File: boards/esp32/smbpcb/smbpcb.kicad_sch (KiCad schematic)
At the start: 69 parts, among them IC1 MiCS-6814, J1 USB_B_Micro, J2 PMS7003, Q1 SUD08P06-155L, Q2 SS8050_NPN, Q3 SS8050_NPN, SW1 RESET, SW2 RESET, U1 MCP73831-2-OT, U2 TPS61200DRC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

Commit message: assembly QOL improvements
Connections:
- net +5V: now also R25.1; no longer R25.2
- net GND: now also D3.1 (K)
- net at D3.2 (A): now also R25.2; no longer R25.1
- net at C5.1, D1.1 (K): no longer D3.1 (K)
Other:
- moved on the sheet: D3, R25
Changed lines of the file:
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@@
   (junction (at 180.34 58.42) (diameter 0.9144) (color 0 0 0 0))
   (junction (at 185.42 80.01) (diameter 0.9144) (color 0 0 0 0))
-  (junction (at 189.23 21.59) (diameter 0.9144) (color 0 0 0 0))
-  (junction (at 189.23 58.42) (diameter 0.9144) (color 0 0 0 0))
   (junction (at 192.405 168.91) (diameter 0.9144) (color 0 0 0 0))
+  (junction (at 198.12 80.01) (diameter 0.9144) (color 0 0 0 0))
   (junction (at 201.93 138.43) (diameter 0.9144) (color 0 0 0 0))
+  (junction (at 212.09 58.42) (diameter 0.9144) (color 0 0 0 0))
   (junction (at 215.265 120.65) (diameter 0.9144) (color 0 0 0 0))
   (junction (at 222.885 120.65) (diameter 0.9144) (color 0 0 0 0))
@@
     (stroke (width 0) (type solid) (color 0 0 0 0))
   )
-  (wire (pts (xy 165.1 21.59) (xy 189.23 21.59))
+  (wire (pts (xy 165.1 21.59) (xy 198.12 21.59))
     (stroke (width 0) (type solid) (color 0 0 0 0))
   )
@@
     (stroke (width 0) (type solid) (color 0 0 0 0))
   )
-  (wire (pts (xy 180.34 58.42) (xy 189.23 58.42))
+  (wire (pts (xy 180.34 58.42) (xy 212.09 58.42))
     (stroke (width 0) (type solid) (color 0 0 0 0))
   )
@@
     (stroke (width 0) (type solid) (color 0 0 0 0))
   )
-  (wire (pts (xy 189.23 21.59) (xy 189.23 33.02))
-    (stroke (width 0) (type solid) (color 0 0 0 0))
-  )
-  (wire (pts (xy 189.23 21.59) (xy 198.12 21.59))
-    (stroke (width 0) (type solid) (color 0 0 0 0))
-  )
-  (wire (pts (xy 189.23 40.64) (xy 189.23 44.45))
-    (stroke (width 0) (type solid) (color 0 0 0 0))
-  )
-  (wire (pts (xy 189.23 52.07) (xy 189.23 58.42))
-    (stroke (width 0) (type solid) (color 0 0 0 0))
-  )
-  (wire (pts (xy 189.23 58.42) (xy 215.9 58.42))
-    (stroke (width 0) (type solid) (color 0 0 0 0))
-  )
   (wire (pts (xy 189.23 135.89) (xy 189.23 139.7))
     (stroke (width 0) (type solid) (color 0 0 0 0))
@@
     (stroke (width 0) (type solid) (color 0 0 0 0))
   )
+  (wire (pts (xy 198.12 82.55) (xy 198.12 80.01))
+    (stroke (width 0) (type solid) (color 0 0 0 0))
+  )
   (wire (pts (xy 199.39 135.89) (xy 199.39 139.7))
     (stroke (width 0) (type solid) (color 0 0 0 0))
@@
   )
   (wire (pts (xy 201.93 168.91) (xy 205.74 168.91))
+    (stroke (width 0) (type solid) (color 0 0 0 0))
+  )
+  (wire (pts (xy 212.09 58.42) (xy 212.09 64.77))
+    (stroke (width 0) (type solid) (color 0 0 0 0))
+  )
+  (wire (pts (xy 212.09 58.42) (xy 215.9 58.42))
+    (stroke (width 0) (type solid) (color 0 0 0 0))
+  )
+  (wire (pts (xy 212.09 72.39) (xy 212.09 74.93))
+    (stroke (width 0) (type solid) (color 0 0 0 0))
+  )
+  (wire (pts (xy 212.09 82.55) (xy 198.12 82.55))
     (stroke (width 0) (type solid) (color 0 0 0 0))
   )
@@
     (pin "2")
   )
-  (symbol (lib_id "Device:R") (at 189.23 48.26 0) (unit 1)
-    (in_bom yes) (on_board yes)
-    (property "Reference" "R25" (id 0) (at 189.865 44.45 0)
-      (effects (font (size 1.27 1.27)) (justify left))
-    )
-    (property "Value" "2k" (id 1) (at 189.865 52.07 0)
-      (effects (font (size 1.27 1.27)) (justify left))
-    )
-    (property "Footprint" "Capacitor_SMD:C_0805_2012Metric" (id 2) (at 187.452 48.26 90)
-      (effects (font (size 1.27 1.27)) hide)
-    )
-    (property "Datasheet" "~" (id 3) (at 189.23 48.26 0)
-      (effects (font (size 1.27 1.27)) hide)
-    )
-    (property "LCSC" "C328391" (id 4) (at 189.23 48.26 0)
-      (effects (font (size 1.27 1.27)) hide)
-    )
-    (property "Mouser" "AECR0805F2K00K9" (id 5) (at 189.23 48.26 0)
-      (effects (font (size 1.27 1.27)) hide)
-    )
-    (pin "1")
-    (pin "2")
-  )
   (symbol (lib_id "Device:R") (at 198.12 168.91 90) (unit 1)
     (in_bom yes) (on_board yes)
@@
     (pin "2")
   )
+  (symbol (lib_id "Device:R") (at 212.09 68.58 0) (unit 1)
+    (in_bom yes) (on_board yes)
+    (property "Reference" "R25" (id 0) (at 212.725 64.77 0)
+      (effects (font (size 1.27 1.27)) (justify left))
+    )
+    (property "Value" "2k" (id 1) (at 212.725 72.39 0)
+      (effects (font (size 1.27 1.27)) (justify left))
+    )
+    (property "Footprint" "Capacitor_SMD:C_0805_2012Metric" (id 2) (at 210.312 68.58 90)
+      (effects (font (size 1.27 1.27)) hide)
+    )
+    (property "Datasheet" "~" (id 3) (at 212.09 68.58 0)
+      (effects (font (size 1.27 1.27)) hide)
+    )
+    (property "LCSC" "C328391" (id 4) (at 212.09 68.58 0)
+      (effects (font (size 1.27 1.27)) hide)
+    )
+    (property "Mouser" "AECR0805F2K00K9" (id 5) (at 212.09 68.58 0)
+      (effects (font (size 1.27 1.27)) hide)
+    )
+    (pin "1")
+    (pin "2")
+  )
   (symbol (lib_id "Device:R") (at 215.265 128.905 0) (unit 1)
     (in_bom yes) (on_board yes)
@@
     (pin "2")
   )
-  (symbol (lib_id "Device:LED") (at 189.23 36.83 270) (unit 1)
-    (in_bom yes) (on_board yes)
-    (property "Reference" "D3" (id 0) (at 191.77 36.195 90)
-      (effects (font (size 1.27 1.27)) (justify left))
-    )
-    (property "Value" "PWR_LED" (id 1) (at 191.77 38.735 90)
-      (effects (font (size 1.27 1.27)) (justify left))
-    )
-    (property "Footprint" "LED_SMD:LED_0805_2012Metric" (id 2) (at 189.23 36.83 0)
-      (effects (font (size 1.27 1.27)) hide)
-    )
-    (property "Datasheet" "~" (id 3) (at 189.23 36.83 0)
-      (effects (font (size 1.27 1.27)) hide)
-    )
-    (property "LCSC" "C72037" (id 4) (at 189.23 36.83 0)
-      (effects (font (size 1.27 1.27)) hide)
-    )
-    (property "Mouser" " 755-SML-H12U8TT86C " (id 5) (at 189.23 36.83 0)
-      (effects (font (size 1.27 1.27)) hide)
-    )
+  (symbol (lib_id "Device:LED") (at 212.09 78.74 90) (unit 1)
+    (in_bom yes) (on_board yes)
+    (property "Reference" "D3" (id 0) (at 209.55 79.375 90)
+      (effects (font (size 1.27 1.27)) (justify left))
+    )
+    (property "Value" "PWR_LED" (id 1) (at 209.55 76.835 90)
+      (effects (font (size 1.27 1.27)) (justify left))
+    )
+    (property "Footprint" "LED_SMD:LED_0805_2012Metric" (id 2) (at 212.09 78.74 0)
+      (effects (font (size 1.27 1.27)) hide)
+    )
+    (property "Datasheet" "~" (id 3) (at 212.09 78.74 0)
+      (effects (font (size 1.27 1.27)) hide)
+    )
+    (property "LCSC" "C72037" (id 4) (at 212.09 78.74 0)
+      (effects (font (size 1.27 1.27)) hide)
+    )
+    (property "Mouser" " 755-SML-H12U8TT86C " (id 5) (at 212.09 78.74 0)
+      (effects (font (size 1.27 1.27)) hide)
+    )

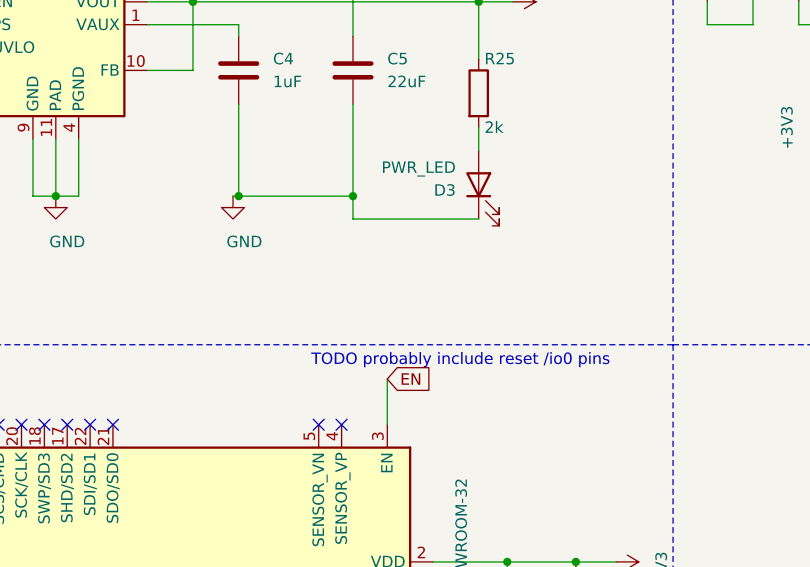
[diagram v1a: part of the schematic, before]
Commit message: wrong micro usb footprint
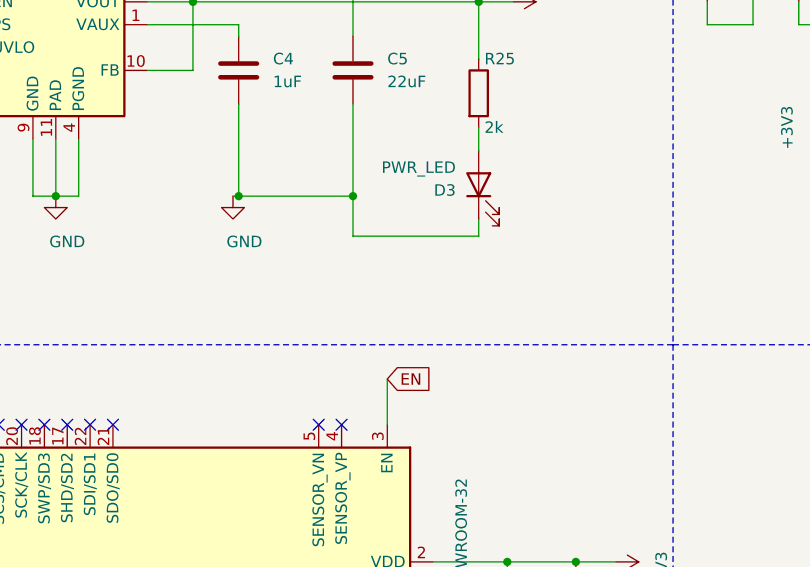
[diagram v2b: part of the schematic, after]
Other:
- note removed: "TODO probably include reset /io0 pins"
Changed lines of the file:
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@@
     (stroke (width 0) (type solid) (color 0 0 0 0))
   )
-  (wire (pts (xy 198.12 82.55) (xy 198.12 80.01))
+  (wire (pts (xy 198.12 80.01) (xy 198.12 84.455))
     (stroke (width 0) (type solid) (color 0 0 0 0))
   )
@@
     (stroke (width 0) (type solid) (color 0 0 0 0))
   )
-  (wire (pts (xy 212.09 82.55) (xy 198.12 82.55))
+  (wire (pts (xy 212.09 82.55) (xy 212.09 84.455))
+    (stroke (width 0) (type solid) (color 0 0 0 0))
+  )
+  (wire (pts (xy 212.09 84.455) (xy 198.12 84.455))
     (stroke (width 0) (type solid) (color 0 0 0 0))
   )
@@
     (effects (font (size 1.27 1.27)) (justify right bottom))
   )
-  (text "TODO probably include reset /io0 pins\n" (at 226.695 99.06 180)
-    (effects (font (size 1.27 1.27)) (justify right bottom))
-  )

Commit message: forgot to save
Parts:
- J1: footprint Connector_USB:USB_Micro-B_GCT_USB3076-30-A -> Connector_USB:USB_Micro-B_Molex-105017-0001
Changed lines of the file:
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@@
     (property "Reference" "J1" (id 0) (at 18.415 47.625 0))
     (property "Value" "USB_B_Micro" (id 1) (at 25.4 47.625 0))
-    (property "Footprint" "Connector_USB:USB_Micro-B_GCT_USB3076-30-A" (id 2) (at 27.305 58.42 0)
+    (property "Footprint" "Connector_USB:USB_Micro-B_Molex-105017-0001" (id 2) (at 27.305 58.42 0)
       (effects (font (size 1.27 1.27)) hide)
     )
@@
     )
     (path "/1f43e278-2549-4f3e-b9ae-cade2ad4d2f1"
-      (reference "J1") (unit 1) (value "USB_B_Micro") (footprint "Connector_USB:USB_Micro-B_GCT_USB3076-30-A")
+      (reference "J1") (unit 1) (value "USB_B_Micro") (footprint "Connector_USB:USB_Micro-B_Molex-105017-0001")
     )
     (path "/b0e046e6-ec2b-40de-9094-a14033950a59"

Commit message: v1 probably
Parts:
- removed C11, C14: 10uF, Capacitor_SMD:C_0805_2012Metric, symbol Device:C
- removed R21: 330k, Capacitor_SMD:C_0805_2012Metric, symbol Device:R
- removed R7, R8, R9: 10k, Capacitor_SMD:C_0805_2012Metric, symbol Device:R
- removed U2: TPS61200DRC, Package_SON:Texas_S-PVSON-N10_ThermalVias, symbol Regulator_Switching:TPS61200DRC
- added C9: 10uF, Capacitor_SMD:C_0805_2012Metric, symbol Device:C
- added R5: 10k, Capacitor_SMD:C_0805_2012Metric, symbol Device:R
- added R6: 330k, Capacitor_SMD:C_0805_2012Metric, symbol Device:R
- added U2: SGM6603-5.0YN6G_TR, Package_TO_SOT_SMD:SOT-23-6, symbol Driver_FET:LTC4440ES6
- C10: value 1uF -> 10uF; LCSC C28323 -> C40894; Mouser 187-CL21B105KBFNNNE -> 0805X106K250NT
- C12, C13: LCSC C49678 -> C495959; Mouser CC0805KRX7R9BB104 -> C0805X104K101TB
- C3: value 4.7uF -> 10uF
- C4: value 1uF -> 10uF; footprint Capacitor_SMD:C_0805_2012Metric -> Capacitor_SMD:C_1206_3216Metric; LCSC C28323 -> C412617; Mouser 187-CL21B105KBFNNNE -> 963-UMJ316BC7475KLHT
- C5: value 22uF -> 1uF; LCSC C45783 -> C28323; Mouser 187-CL21A226MAQNNNE -> 187-CL21B105KBFNNNE
- L1: value 2.2uH -> 4.7uH; LCSC C1043 -> C479902; Mouser 652-CVH201205-2R2M -> SCMI201209U4R7KT
- R17, R18: LCSC C844941 -> C269733; Mouser CRCW08054K70FKEA -> RMC08054.7K5%N
- R2: value 2M -> 10k; LCSC C325853 -> C269724; Mouser RMC08052M5%N -> 71-TNPU080510K0AWEN
- R3: value 180k -> 10k; LCSC C352261 -> C269724; Mouser AECR0805F180KK9 -> 71-TNPU080510K0AWEN
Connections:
- net +3V3: now also C7.1, R17.1, R18.1, R2.1, R3.1, R5.1; no longer C10.1, R17.2, R18.2
- net +5V: now also C4.1, D1.1 (K), U2.5 (VOUT)
- net GND: now also C10.1, C7.2, C9.1, R6.1, U2.2 (GND); no longer C10.2, C5.2, R3.2
- net SCL: now also R18.2, R3.2; no longer R18.1
- net SDA: now also R17.2, R5.2; no longer R17.1
- net at U4.9 (~RES): now also R2.2
- net at C3.1, L1.1, Q1.2 (D): now also U2.3 (EN), U2.6 (VCC); no longer R2.1
- net at C5.1: now also U4.1 (C2P); no longer D1.1 (K)
- net at U4.13 (VCOMH): now also C9.2
- net at U4.3 (C1P): now also C6.1; no longer C7.1
- net at U4.4 (C1N): now also C6.2; no longer C7.2
- net at U4.14 (VCC): now also C10.2
- net at L1.2: now also U2.1 (SW)
- net at U4.12 (IREF): now also R6.2
- net at U4.2 (C2N): now also C5.2; no longer C6.2
- no-connect marks 27 -> 28
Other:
- note added: "address = 0x76"
- moved on the sheet: C3, L1, R17, R18
